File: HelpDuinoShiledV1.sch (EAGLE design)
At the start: 30 parts

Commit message: adding traces
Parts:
- removed LSP10, LSP11, LSP12, LSP14, LSP15, LSP16, LSP17, LSP18, LSP19, LSP20, LSP21, LSP22, LSP23, LSP5, LSP6, LSP7, LSP8, LSP9: SE13, solpad:SE13
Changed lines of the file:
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@@
 <part name="LSP3" library="solpad" deviceset="SE13" device=""/>
 <part name="LSP4" library="solpad" deviceset="SE13" device=""/>
-<part name="LSP5" library="solpad" deviceset="SE13" device=""/>
-<part name="LSP6" library="solpad" deviceset="SE13" device=""/>
-<part name="LSP7" library="solpad" deviceset="SE13" device=""/>
-<part name="LSP8" library="solpad" deviceset="SE13" device=""/>
-<part name="LSP9" library="solpad" deviceset="SE13" device=""/>
-<part name="LSP10" library="solpad" deviceset="SE13" device=""/>
-<part name="LSP11" library="solpad" deviceset="SE13" device=""/>
-<part name="LSP12" library="solpad" deviceset="SE13" device=""/>
 <part name="LSP13" library="solpad" deviceset="SE13" device=""/>
-<part name="LSP14" library="solpad" deviceset="SE13" device=""/>
-<part name="LSP15" library="solpad" deviceset="SE13" device=""/>
-<part name="LSP16" library="solpad" deviceset="SE13" device=""/>
-<part name="LSP17" library="solpad" deviceset="SE13" device=""/>
-<part name="LSP18" library="solpad" deviceset="SE13" device=""/>
-<part name="LSP19" library="solpad" deviceset="SE13" device=""/>
-<part name="LSP20" library="solpad" deviceset="SE13" device=""/>
-<part name="LSP21" library="solpad" deviceset="SE13" device=""/>
-<part name="LSP22" library="solpad" deviceset="SE13" device=""/>
-<part name="LSP23" library="solpad" deviceset="SE13" device=""/>
 </parts>
 <sheets>
@@
 <instance part="LSP3" gate="1" x="58.42" y="-25.4"/>
 <instance part="LSP4" gate="1" x="63.5" y="-25.4"/>
-<instance part="LSP5" gate="1" x="68.58" y="-25.4"/>
-<instance part="LSP6" gate="1" x="73.66" y="-25.4"/>
-<instance part="LSP7" gate="1" x="78.74" y="-25.4"/>
-<instance part="LSP8" gate="1" x="83.82" y="-25.4"/>
-<instance part="LSP9" gate="1" x="48.26" y="-33.02"/>
-<instance part="LSP10" gate="1" x="53.34" y="-33.02"/>
-<instance part="LSP11" gate="1" x="58.42" y="-33.02"/>
-<instance part="LSP12" gate="1" x="63.5" y="-33.02"/>
 <instance part="LSP13" gate="1" x="68.58" y="-33.02"/>
-<instance part="LSP14" gate="1" x="73.66" y="-33.02"/>
-<instance part="LSP15" gate="1" x="76.2" y="-33.02"/>
-<instance part="LSP16" gate="1" x="78.74" y="-33.02"/>
-<instance part="LSP17" gate="1" x="81.28" y="-33.02"/>
-<instance part="LSP18" gate="1" x="83.82" y="-33.02"/>
-<instance part="LSP19" gate="1" x="86.36" y="-33.02"/>
-<instance part="LSP20" gate="1" x="91.44" y="-30.48"/>
-<instance part="LSP21" gate="1" x="96.52" y="-30.48"/>
-<instance part="LSP22" gate="1" x="101.6" y="-27.94"/>
-<instance part="LSP23" gate="1" x="104.14" y="-27.94"/>
 </instances>
 <busses>

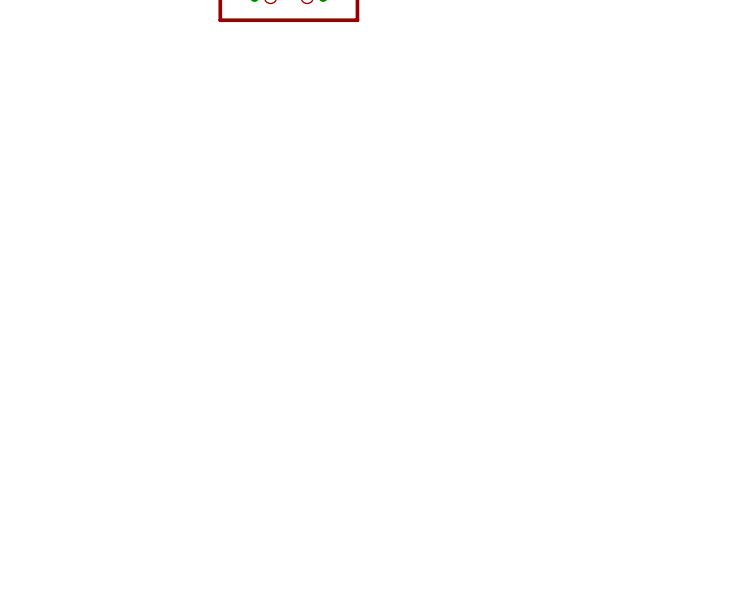
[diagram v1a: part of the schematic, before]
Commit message: added 3.3v
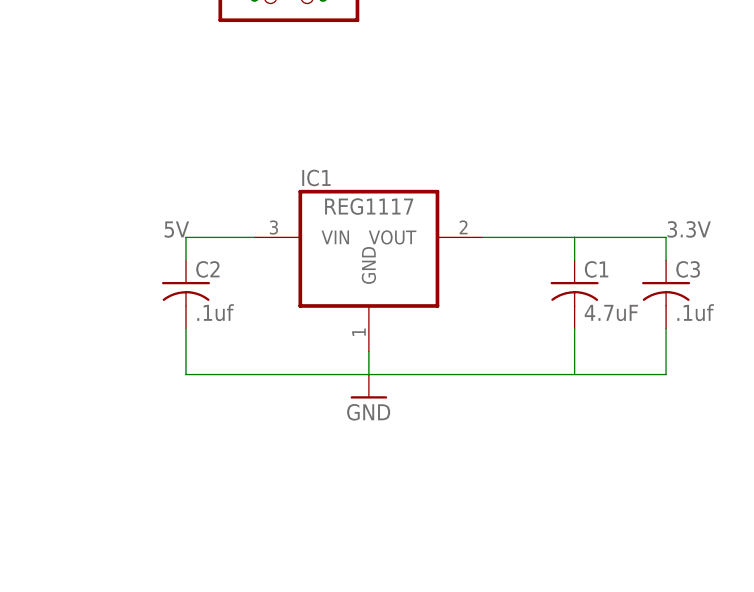
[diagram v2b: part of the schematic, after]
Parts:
- added C1: 4.7uF, rcl:C-USC0603K
- added C2, C3: .1uf, rcl:C-USC0603K
- added IC1: REG1117, burr-brown:REG1117
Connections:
- new net 3.3V: C1.1, C3.1, IC1.VOUT
- net 5V: now also C2.1, IC1.VIN
- net GND: now also C1.2, C2.2, C3.2, IC1.GND
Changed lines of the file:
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@@
 <part name="LSP4" library="solpad" deviceset="SE13" device=""/>
 <part name="LSP13" library="solpad" deviceset="SE13" device=""/>
+<part name="IC1" library="burr-brown" deviceset="REG1117" device=""/>
+<part name="C1" library="rcl" deviceset="C-US" device="C0603K" value="4.7uF"/>
+<part name="C2" library="rcl" deviceset="C-US" device="C0603K" value=".1uf"/>
+<part name="C3" library="rcl" deviceset="C-US" device="C0603K" value=".1uf"/>
+<part name="GND1" library="supply1" deviceset="GND" device=""/>
 </parts>
 <sheets>
@@
 <instance part="LSP4" gate="1" x="63.5" y="-25.4"/>
 <instance part="LSP13" gate="1" x="68.58" y="-33.02"/>
+<instance part="IC1" gate="G$1" x="220.98" y="30.48"/>
+<instance part="C1" gate="G$1" x="243.84" y="25.4"/>
+<instance part="C2" gate="G$1" x="200.66" y="25.4"/>
+<instance part="C3" gate="G$1" x="254" y="25.4"/>
+<instance part="GND1" gate="1" x="220.98" y="12.7"/>
 </instances>
 <busses>
@@
 <label x="55.88" y="33.02" size="1.27" layer="95" ratio="10"/>
 </segment>
+<segment>
+<pinref part="IC1" gate="G$1" pin="GND"/>
+<pinref part="GND1" gate="1" pin="GND"/>
+<pinref part="C1" gate="G$1" pin="2"/>
+<wire x1="220.98" y1="15.24" x2="243.84" y2="15.24" width="0.1524" layer="91"/>
+<wire x1="243.84" y1="15.24" x2="243.84" y2="20.32" width="0.1524" layer="91"/>
+<pinref part="C3" gate="G$1" pin="2"/>
+<wire x1="243.84" y1="15.24" x2="254" y2="15.24" width="0.1524" layer="91"/>
+<wire x1="254" y1="15.24" x2="254" y2="20.32" width="0.1524" layer="91"/>
+<pinref part="C2" gate="G$1" pin="2"/>
+<wire x1="200.66" y1="20.32" x2="200.66" y2="15.24" width="0.1524" layer="91"/>
+<wire x1="200.66" y1="15.24" x2="220.98" y2="15.24" width="0.1524" layer="91"/>
+<wire x1="220.98" y1="15.24" x2="220.98" y2="17.78" width="0.1524" layer="91"/>
+</segment>
 </net>
 <net name="3V3" class="0">
@@
 <label x="55.88" y="45.72" size="1.27" layer="95" ratio="10"/>
 </segment>
+<segment>
+<pinref part="IC1" gate="G$1" pin="VIN"/>
+<pinref part="C2" gate="G$1" pin="1"/>
+<wire x1="208.28" y1="30.48" x2="200.66" y2="30.48" width="0.1524" layer="91"/>
+<wire x1="200.66" y1="30.48" x2="200.66" y2="27.94" width="0.1524" layer="91"/>
+<label x="198.12" y="30.48" size="1.778" layer="95"/>
+</segment>
 </net>
 <net name="MISO" class="0">
@@
 </segment>
 </net>
+<net name="3.3V" class="0">
+<segment>
+<pinref part="IC1" gate="G$1" pin="VOUT"/>
+<pinref part="C1" gate="G$1" pin="1"/>
+<wire x1="233.68" y1="30.48" x2="243.84" y2="30.48" width="0.1524" layer="91"/>
+<wire x1="243.84" y1="27.94" x2="243.84" y2="30.48" width="0.1524" layer="91"/>
+<pinref part="C3" gate="G$1" pin="1"/>
+<wire x1="243.84" y1="30.48" x2="254" y2="30.48" width="0.1524" layer="91"/>
+<wire x1="254" y1="30.48" x2="254" y2="27.94" width="0.1524" layer="91"/>
+<label x="254" y="30.48" size="1.778" layer="95"/>
+</segment>
+</net>
